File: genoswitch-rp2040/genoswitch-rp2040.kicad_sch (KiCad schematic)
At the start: 40 parts, among them J1 USB_B_Micro, J10 RP2040_ADC2, J11 RP2040_ADC3, J2 Conn_01x03_Socket-PicoDebug, J3 HW-SPI0, J4 HW-SPI1, J5 PIO-SPI0, J6 PIO-SPI1, J7 SERIAL, J8 RP2040_ADC0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

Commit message: Revert "Change 0603 components to 0402 sizes"
This reverts commit b164c8e7de76090c9848900fff1e32a63cc8b3a4.
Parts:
- C1, C10, C101, C11, C12, C13, C14, C15, C16, C4, C6, C7, C8, C9: footprint Capacitor_SMD:C_01005_0402Metric -> Capacitor_SMD:C_0201_0603Metric
- R1, R2, R3, R4, R5: footprint Resistor_SMD:R_01005_0402Metric -> Resistor_SMD:R_0201_0603Metric
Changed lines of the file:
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@@
       (effects (font (size 1.27 1.27)) (justify left))
     )
-    (property "Footprint" "Capacitor_SMD:C_01005_0402Metric" (at 70.8152 31.75 0)
+    (property "Footprint" "Capacitor_SMD:C_0201_0603Metric" (at 70.8152 31.75 0)
       (effects (font (size 1.27 1.27)) hide)
     )
@@
       (effects (font (size 1.27 1.27)) (justify left))
     )
-    (property "Footprint" "Resistor_SMD:R_01005_0402Metric" (at 168.402 25.4 90)
+    (property "Footprint" "Resistor_SMD:R_0201_0603Metric" (at 168.402 25.4 90)
       (effects (font (size 1.27 1.27)) hide)
     )
@@
       (effects (font (size 1.27 1.27)) (justify left))
     )
-    (property "Footprint" "Resistor_SMD:R_01005_0402Metric" (at 168.402 35.56 90)
+    (property "Footprint" "Resistor_SMD:R_0201_0603Metric" (at 168.402 35.56 90)
       (effects (font (size 1.27 1.27)) hide)
     )
@@
       (effects (font (size 1.27 1.27)))
     )
-    (property "Footprint" "Resistor_SMD:R_01005_0402Metric" (at 349.25 178.308 90)
+    (property "Footprint" "Resistor_SMD:R_0201_0603Metric" (at 349.25 178.308 90)
       (effects (font (size 1.27 1.27)) hide)
     )
@@
       (effects (font (size 1.27 1.27)) (justify left))
     )
-    (property "Footprint" "Capacitor_SMD:C_01005_0402Metric" (at 108.9152 31.75 0)
+    (property "Footprint" "Capacitor_SMD:C_0201_0603Metric" (at 108.9152 31.75 0)
       (effects (font (size 1.27 1.27)) hide)
     )
@@
       (effects (font (size 1.27 1.27)) (justify left))
     )
-    (property "Footprint" "Capacitor_SMD:C_01005_0402Metric" (at 39.0652 31.75 0)
+    (property "Footprint" "Capacitor_SMD:C_0201_0603Metric" (at 39.0652 31.75 0)
       (effects (font (size 1.27 1.27)) hide)
     )
@@
       (effects (font (size 1.27 1.27)))
     )
-    (property "Footprint" "Resistor_SMD:R_01005_0402Metric" (at 351.79 38.862 90)
+    (property "Footprint" "Resistor_SMD:R_0201_0603Metric" (at 351.79 38.862 90)
       (effects (font (size 1.27 1.27)) hide)
     )
@@
       (effects (font (size 1.27 1.27)) (justify right))
     )
-    (property "Footprint" "Capacitor_SMD:C_01005_0402Metric" (at 190.8048 179.07 0)
+    (property "Footprint" "Capacitor_SMD:C_0201_0603Metric" (at 190.8048 179.07 0)
       (effects (font (size 1.27 1.27)) hide)
     )
@@
       (effects (font (size 1.27 1.27)) (justify left))
     )
-    (property "Footprint" "Capacitor_SMD:C_01005_0402Metric" (at 51.7652 44.45 0)
+    (property "Footprint" "Capacitor_SMD:C_0201_0603Metric" (at 51.7652 44.45 0)
       (effects (font (size 1.27 1.27)) hide)
     )
@@
       (effects (font (size 1.27 1.27)) (justify left))
     )
-    (property "Footprint" "Capacitor_SMD:C_01005_0402Metric" (at 171.1452 49.53 0)
+    (property "Footprint" "Capacitor_SMD:C_0201_0603Metric" (at 171.1452 49.53 0)
       (effects (font (size 1.27 1.27)) hide)
     )
@@
       (effects (font (size 1.27 1.27)) (justify left))
     )
-    (property "Footprint" "Capacitor_SMD:C_01005_0402Metric" (at 53.0352 31.75 0)
+    (property "Footprint" "Capacitor_SMD:C_0201_0603Metric" (at 53.0352 31.75 0)
       (effects (font (size 1.27 1.27)) hide)
     )
@@
       (effects (font (size 1.27 1.27)) (justify left))
     )
-    (property "Footprint" "Capacitor_SMD:C_01005_0402Metric" (at 398.4752 231.14 0)
+    (property "Footprint" "Capacitor_SMD:C_0201_0603Metric" (at 398.4752 231.14 0)
       (effects (font (size 1.27 1.27)) hide)
     )
@@
       (effects (font (size 1.27 1.27)) (justify left))
     )
-    (property "Footprint" "Capacitor_SMD:C_01005_0402Metric" (at 107.6452 53.34 0)
+    (property "Footprint" "Capacitor_SMD:C_0201_0603Metric" (at 107.6452 53.34 0)
       (effects (font (size 1.27 1.27)) hide)
     )
@@
       (effects (font (size 1.27 1.27)) (justify left))
     )
-    (property "Footprint" "Capacitor_SMD:C_01005_0402Metric" (at 121.6152 31.75 0)
+    (property "Footprint" "Capacitor_SMD:C_0201_0603Metric" (at 121.6152 31.75 0)
       (effects (font (size 1.27 1.27)) hide)
     )
@@
       (effects (font (size 1.27 1.27)) (justify left))
     )
-    (property "Footprint" "Capacitor_SMD:C_01005_0402Metric" (at 96.2152 31.75 0)
+    (property "Footprint" "Capacitor_SMD:C_0201_0603Metric" (at 96.2152 31.75 0)
       (effects (font (size 1.27 1.27)) hide)
     )
@@
       (effects (font (size 1.27 1.27)) (justify left))
     )
-    (property "Footprint" "Capacitor_SMD:C_01005_0402Metric" (at 83.5152 31.75 0)
+    (property "Footprint" "Capacitor_SMD:C_0201_0603Metric" (at 83.5152 31.75 0)
       (effects (font (size 1.27 1.27)) hide)
     )
@@
       (effects (font (size 1.27 1.27)) (justify left))
     )
-    (property "Footprint" "Capacitor_SMD:C_01005_0402Metric" (at 329.8952 231.14 0)
+    (property "Footprint" "Capacitor_SMD:C_0201_0603Metric" (at 329.8952 231.14 0)
       (effects (font (size 1.27 1.27)) hide)
     )
@@
       (effects (font (size 1.27 1.27)) (justify right))
     )
-    (property "Footprint" "Resistor_SMD:R_01005_0402Metric" (at 367.538 35.56 90)
+    (property "Footprint" "Resistor_SMD:R_0201_0603Metric" (at 367.538 35.56 90)
       (effects (font (size 1.27 1.27)) hide)
     )
@@
       (effects (font (size 1.27 1.27)) (justify left))
     )
-    (property "Footprint" "Capacitor_SMD:C_01005_0402Metric" (at 134.3152 31.75 0)
-      (effects (font (size 1.27 1.27)) hide)
-    )
+    (property "Footprint" "Capacitor_SMD:C_0201_0603Metric" (at 134.3152 31.75 0)
+      (effects (font (size 1.27 1.27)) hide)
+    )

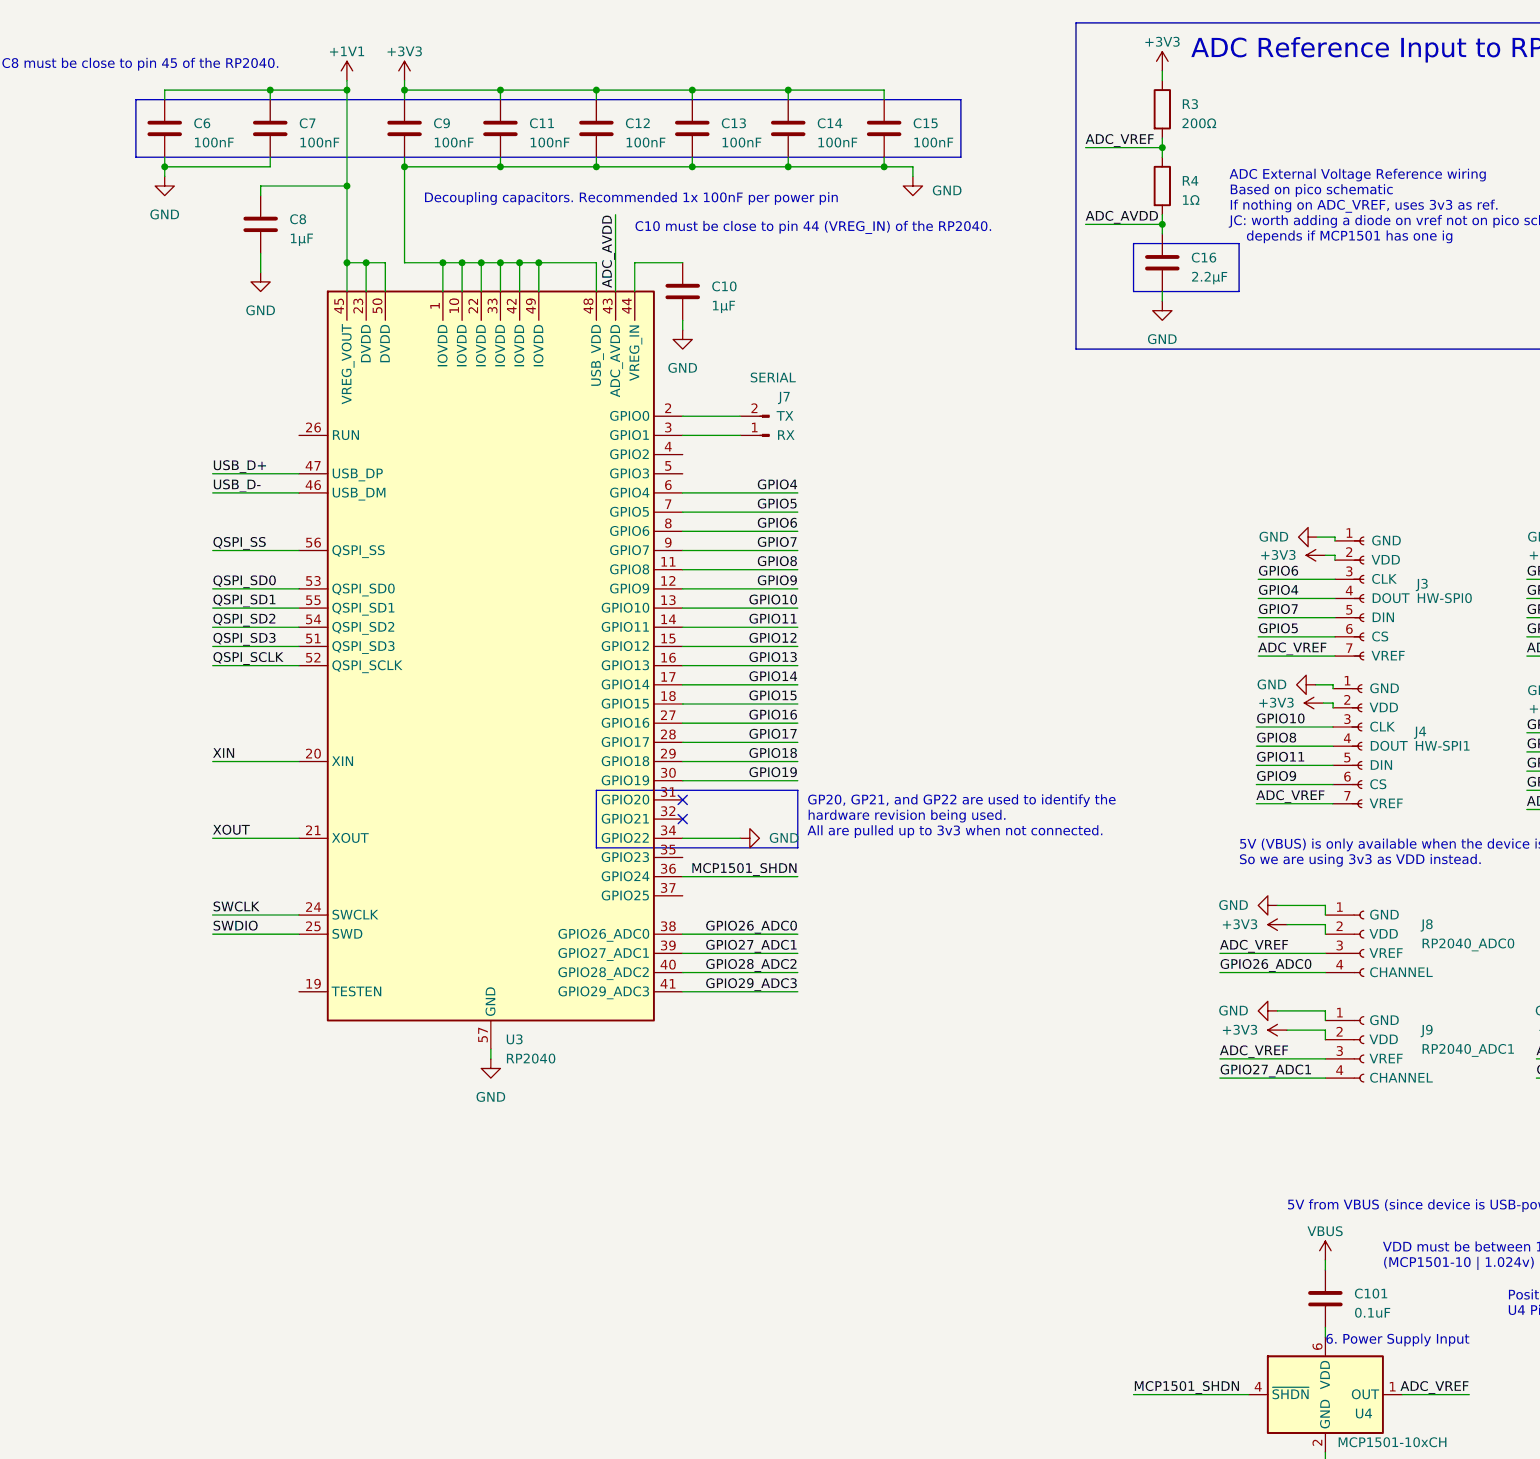
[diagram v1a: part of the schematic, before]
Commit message: Add missing decoupling cap for 7th power pin, renumber C16->C17, C101->C18
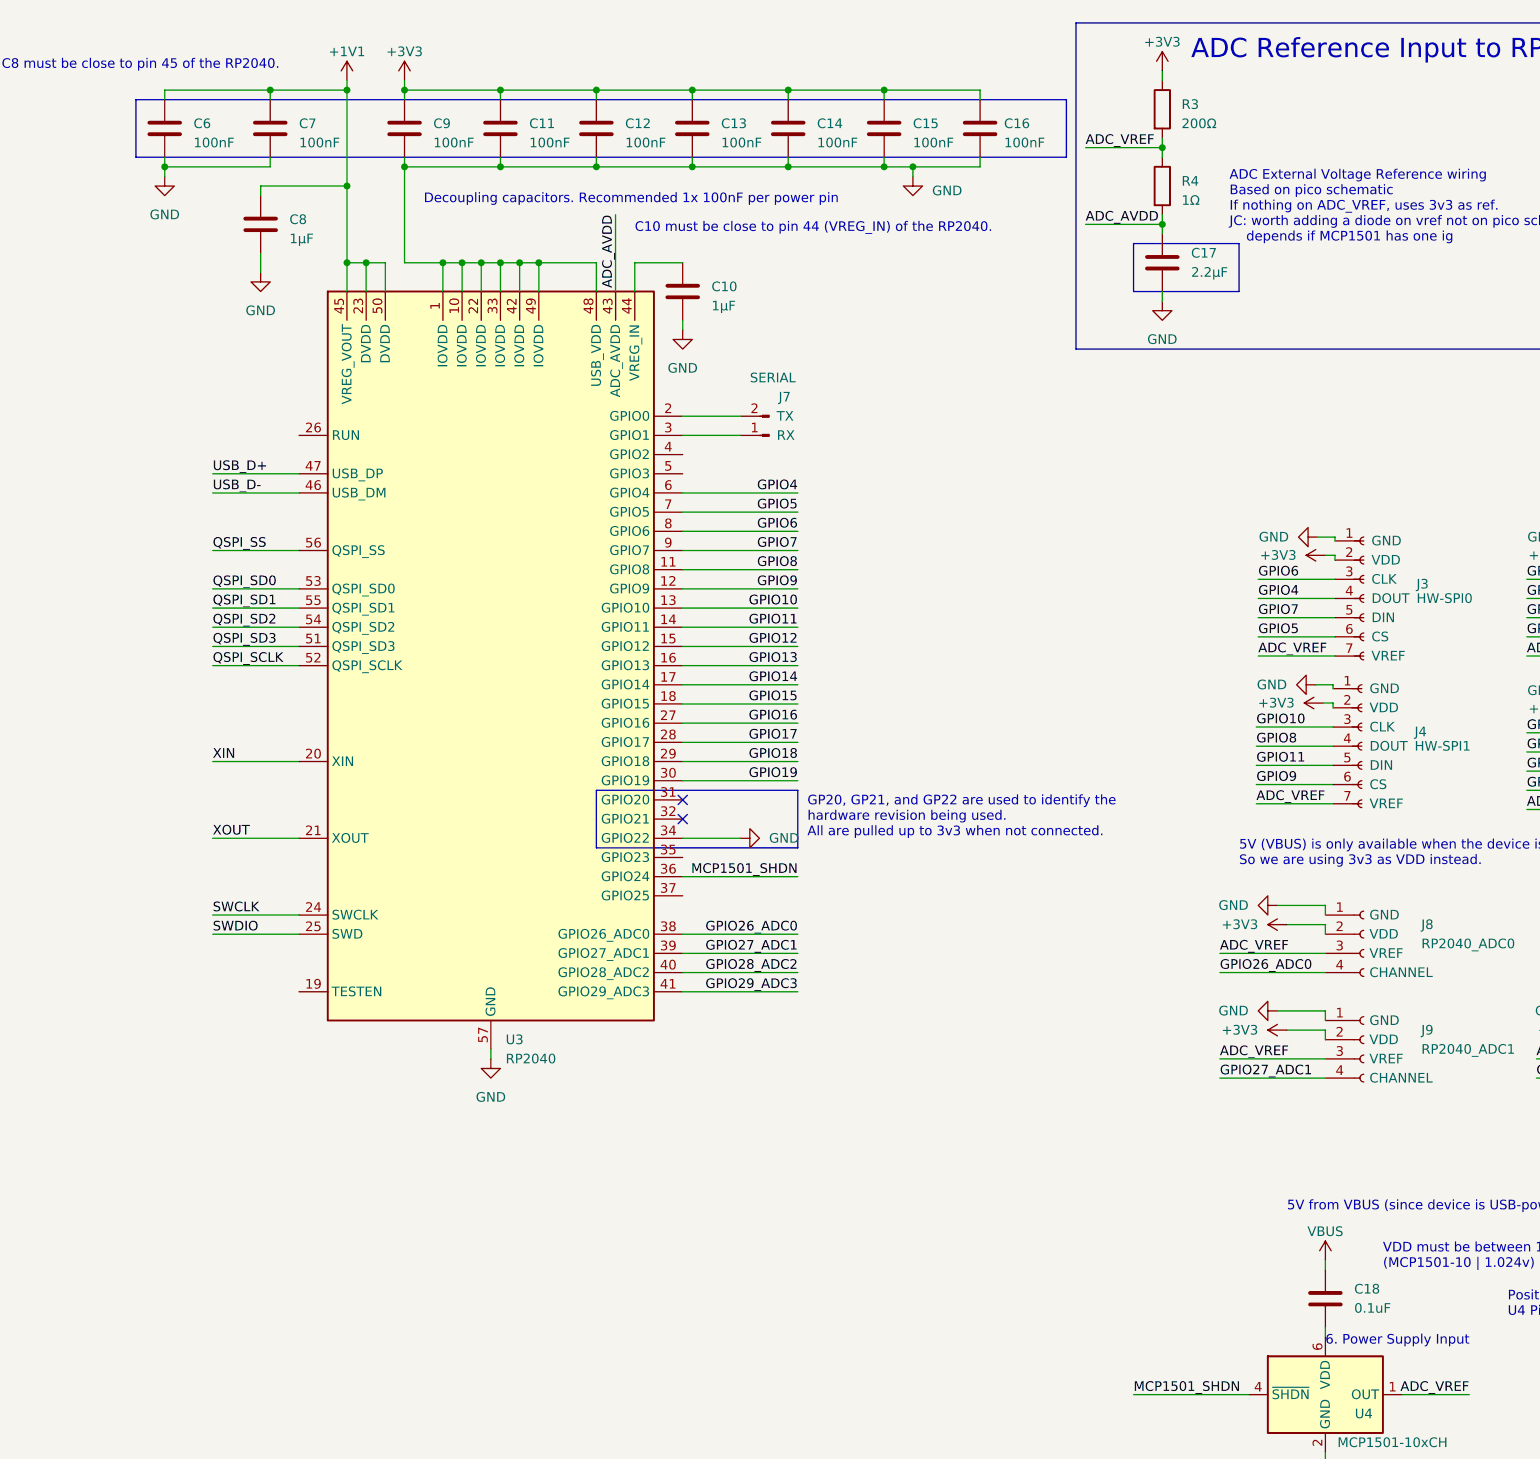
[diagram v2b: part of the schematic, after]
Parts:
- added C16: 100nF, Capacitor_SMD:C_0201_0603Metric, symbol Device:C
- renumbered C16 to C17, C101 to C18
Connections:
- net +3V3: now also C16.1
- net GND: now also C16.2
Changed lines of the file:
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@@
   (junction (at 95.25 22.86) (diameter 0) (color 0 0 0 0)
   )
+  (junction (at 137.16 33.02) (diameter 0) (color 0 0 0 0)
+  )
   (junction (at 77.47 45.72) (diameter 0) (color 0 0 0 0)
   )
@@
   )
   (junction (at 120.65 22.86) (diameter 0) (color 0 0 0 0)
+  )
+  (junction (at 133.35 22.86) (diameter 0) (color 0 0 0 0)
   )
   (junction (at 107.95 22.86) (diameter 0) (color 0 0 0 0)
@@
     (stroke (width 0) (type default))
   )
+  (wire (pts (xy 146.05 33.02) (xy 137.16 33.02))
+    (stroke (width 0) (type default))
+  )
   (wire (pts (xy 191.516 104.013) (xy 192.786 104.013))
     (stroke (width 0) (type default))
@@
     (stroke (width 0) (type default))
   )
+  (wire (pts (xy 146.05 24.13) (xy 146.05 22.86))
+    (stroke (width 0) (type default))
+  )
   (wire (pts (xy 166.37 195.58) (xy 181.61 195.58))
     (stroke (width 0) (type default))
@@
     (stroke (width 0) (type default))
   )
+  (wire (pts (xy 146.05 22.86) (xy 133.35 22.86))
+    (stroke (width 0) (type default))
+  )
   (wire (pts (xy 355.6 40.64) (xy 365.76 40.64))
     (stroke (width 0) (type default))
@@
   )
   (wire (pts (xy 219.71 151.13) (xy 233.68 151.13))
+    (stroke (width 0) (type default))
+  )
+  (wire (pts (xy 146.05 31.75) (xy 146.05 33.02))
     (stroke (width 0) (type default))
   )
@@
     (fill (type none))
   )
-  (rectangle (start 34.29 24.13) (end 143.51 31.75)
+  (rectangle (start 34.29 24.13) (end 157.48 31.75)
     (stroke (width 0) (type default) (color 255 153 0 1))
     (fill (type none))
@@
   (symbol (lib_id "Device:C") (at 191.77 182.88 180) (unit 1)
     (in_bom yes) (on_board yes) (dnp no) (fields_autoplaced)
-    (property "Reference" "C101" (at 195.58 182.245 0)
+    (property "Reference" "C18" (at 195.58 181.61 0)
       (effects (font (size 1.27 1.27)) (justify right))
     )
-    (property "Value" "0.1uF" (at 195.58 184.785 0)
+    (property "Value" "0.1uF" (at 195.58 184.15 0)
       (effects (font (size 1.27 1.27)) (justify right))
     )
@@
       (project "genoswitch-rp2040"
         (path "/2e7ee4d9-1204-4a0f-bb2c-fb0f0d4af2cf"
-          (reference "C101") (unit 1)
+          (reference "C18") (unit 1)
         )
       )
@@
   (symbol (lib_id "Device:C") (at 170.18 45.72 0) (unit 1)
     (in_bom yes) (on_board yes) (dnp no) (fields_autoplaced)
-    (property "Reference" "C16" (at 173.99 45.085 0)
-      (effects (font (size 1.27 1.27)) (justify left))
-    )
-    (property "Value" "2.2μF" (at 173.99 47.625 0)
+    (property "Reference" "C17" (at 173.99 44.45 0)
+      (effects (font (size 1.27 1.27)) (justify left))
+    )
+    (property "Value" "2.2μF" (at 173.99 46.99 0)
       (effects (font (size 1.27 1.27)) (justify left))
     )
@@
       (project "genoswitch-rp2040"
         (path "/2e7ee4d9-1204-4a0f-bb2c-fb0f0d4af2cf"
-          (reference "C16") (unit 1)
+          (reference "C17") (unit 1)
         )
       )
@@
         )
       )
+    )
+  )
+  (symbol (lib_id "Device:C") (at 146.05 27.94 0) (unit 1)
+    (in_bom yes) (on_board yes) (dnp no)
+    (property "Reference" "C16" (at 149.225 27.305 0)
+      (effects (font (size 1.27 1.27)) (justify left))
+    )
+    (property "Value" "100nF" (at 149.225 29.845 0)
+      (effects (font (size 1.27 1.27)) (justify left))
+    )
+    (property "Footprint" "Capacitor_SMD:C_0201_0603Metric" (at 147.0152 31.75 0)
+      (effects (font (size 1.27 1.27)) hide)
+    )
+    (property "Datasheet" "~" (at 146.05 27.94 0)
+      (effects (font (size 1.27 1.27)) hide)
+    )
+    (pin "1")
+    (pin "2")
+    (instances
+      (project "genoswitch-rp2040"
+        (path "/2e7ee4d9-1204-4a0f-bb2c-fb0f0d4af2cf"
+          (reference "C16") (unit 1)
+        )
+      )
